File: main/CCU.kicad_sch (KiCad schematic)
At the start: 8 parts, among them U2 ESP32-DevKitC, U27 Oak-D, U4 Waveshare 23721, U5 MPU6050

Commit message: added logos, oranised sheets, final version
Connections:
- new net: A4.3 (I2C1_SDA), ISO17. (VCC), U5. (XDA)
- new net: A4.5 (I2C1_SDL), ISO17. (VCC), U5. (XDA)
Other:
- company: (none) -> Designers: Krzysztof Grajek, Wojtek Kołodziej
- title: (none) -> Central Control Unit schematic
- moved on the sheet: A2, A4A, A4B, D36V6F27, ISO17, U2, U27, U4, U5

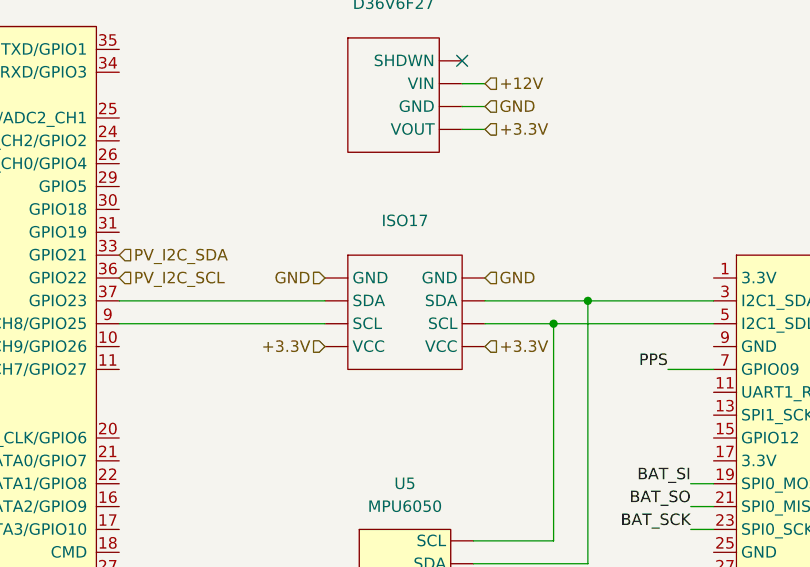
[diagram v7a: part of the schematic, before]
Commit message: Changed name of Adafruit 4903(i2c spearator). Changed values of resistors used in panels
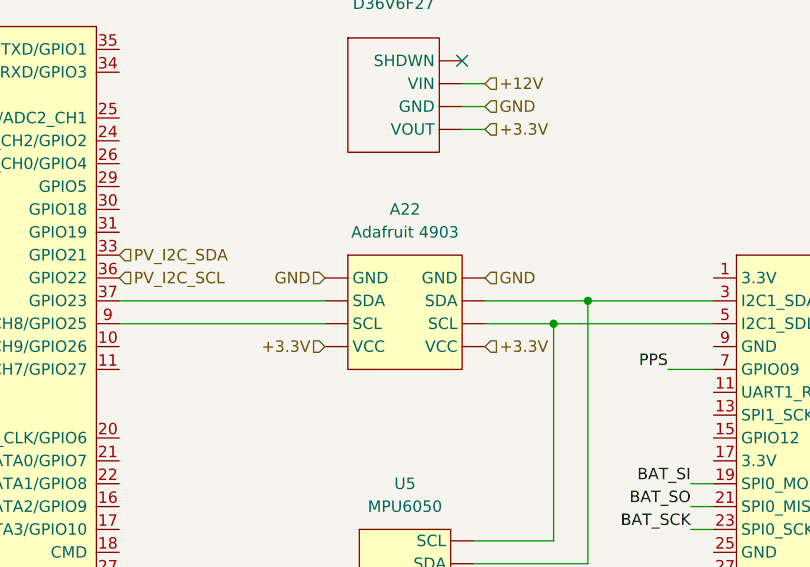
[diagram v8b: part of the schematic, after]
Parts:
- removed ISO17: ~, symbol New_Library_0:Bidirectional I2C Isolator
- added A22: Adafruit 4903, symbol New_Library_0:Adafruit_4903
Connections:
- net +3.3V: now also A22. (VCC)
- net GND: now also A22. (VCC)
- net at A4.3 (I2C1_SDA), U5. (XDA): now also A22. (VCC)
- net at A4.5 (I2C1_SDL), U5. (XDA): now also A22. (VCC)
- net at U2.37 (GPIO23): now also A22. (VCC)
- net at U2.9 (DAC_1/ADC2_CH8/GPIO25): now also A22. (VCC)
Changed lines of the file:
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@@
 	)
 	(symbol
-		(lib_name "Jetson_Orion_Nano_1")
 		(lib_id "New_Library_0:Jetson_Orion_Nano")
 		(at 171.45 120.65 0)
@@
 	)
 	(symbol
-		(lib_id "New_Library_0:Bidirectional I2C Isolator")
+		(lib_id "New_Library_0:Adafruit_4903")
 		(at 118.11 83.82 0)
 		(unit 1)
@@
 		(dnp no)
 		(fields_autoplaced yes)
-		(property "Reference" "ISO17"
-			(at 118.11 73.66 0)
-			(effects
-				(font
-					(size 1.27 1.27)
-				)
-			)
-		)
-		(property "Value" "~"
-			(at 118.11 76.2 0)
+		(property "Reference" "A22"
+			(at 118.11 72.39 0)
+			(effects
+				(font
+					(size 1.27 1.27)
+				)
+			)
+		)
+		(property "Value" "Adafruit 4903"
+			(at 118.11 74.93 0)
 			(effects
 				(font
@@
 			(project "main"
 				(path "/54fbbba9-a737-4199-9a4b-f9fa49b3de5e/2f810269-778d-47ba-b7da-0b431c3bad09"
-					(reference "ISO17")
+					(reference "A22")
 					(unit 1)
 				)
@@
 		(pin "9"
 		)
-		(pin ""
-		)
 		(pin "30"
 		)
@@
 		(pin "33"
 		)
-		(pin ""
-		)
 		(pin "1"
